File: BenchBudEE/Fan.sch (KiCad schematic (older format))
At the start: 0 parts

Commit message: Fan driver block diagram
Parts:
- added Q?: MOSFET_N, ~, symbol MOSFET_N
- added R? (x5): R, ~, symbol R
- added RV?: POT, ~, symbol POT
- added U?: LM324, symbol LM324
- added U?: MCP4922-E/P, DIP14, symbol MCP4922-E/P
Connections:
- net Fan_In: now also R?.2, R?.2
- net Power+: now also Q?.S
- new net: Q?.G, U?.1
- new net: R?.1, R?.2, R?.2, RV?.3, U?.3 (+)
- new net: R?.1, U?.14 (VoutA)
- new net: R?.1, U?.9 (~SHDN~)
- new net +12V: Q?.D, R?.1, U?.4 (V+)
- new net -12V: U?.11 (V-)
- new net AGND: R?.2, RV?.1
- new net CS_N: U?.3 (~CS~)
- new net Current Measure: R?.1, U?.2 (-)
- new net MOSI: U?.5 (SDI)
- new net SCLK: U?.4 (SCK)

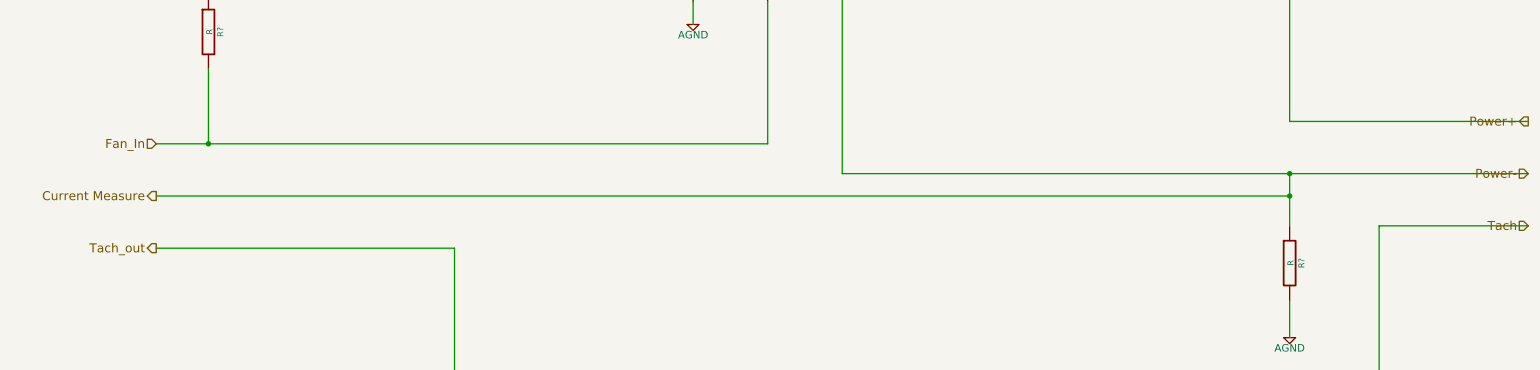
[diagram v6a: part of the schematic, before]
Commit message: Arduino block diagram
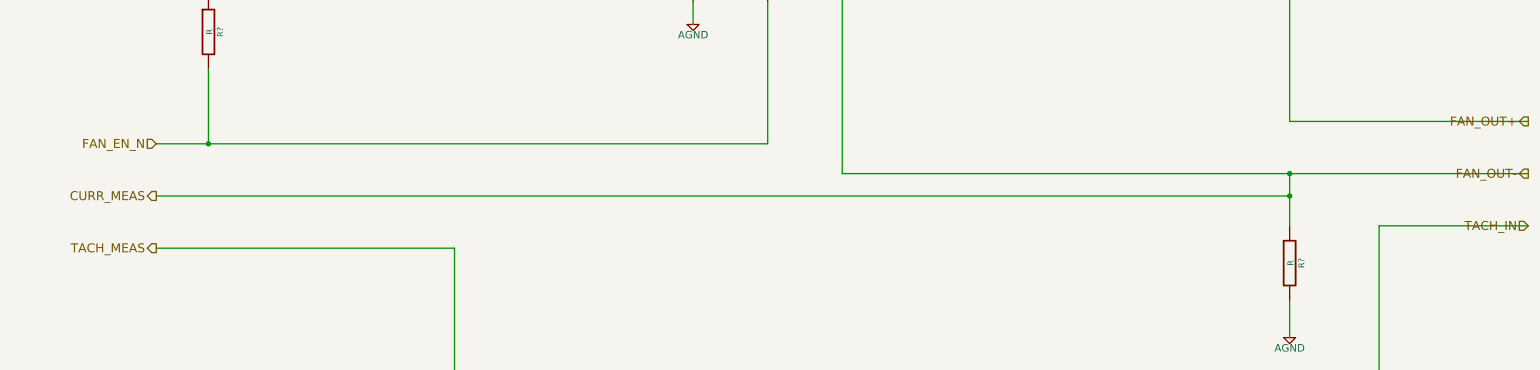
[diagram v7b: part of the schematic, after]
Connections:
- net Current Measure renamed CURR_MEAS
- net Fan_In renamed FAN_EN_N
- net Power+ renamed FAN_OUT+
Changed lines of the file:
@@
 $Descr A4 11693 8268
 encoding utf-8
-Sheet 6 9
+Sheet 8 9
 Title ""
 Date "9 feb 2014"
@@
 $EndDescr
 Text HLabel 10500 4000 0    60   Output ~ 0
-Power+
-Text HLabel 10500 4350 0    60   Input ~ 0
-Power-
+FAN_OUT+
+Text HLabel 10500 4350 0    60   Output ~ 0
+FAN_OUT-
 Text HLabel 10500 4700 0    60   Input ~ 0
-Tach
+TACH_IN
 Text HLabel 1300 4850 0    60   Output ~ 0
-Tach_out
+TACH_MEAS
 Text HLabel 1300 4150 0    60   Input ~ 0
-Fan_In
+FAN_EN_N
 $Comp
 L LM324 U?
@@
 	3300 4850 1300 4850
 Text HLabel 1300 4500 0    60   Output ~ 0
-Current Measure
+CURR_MEAS
 Wire Wire Line
 	8900 4500 1300 4500

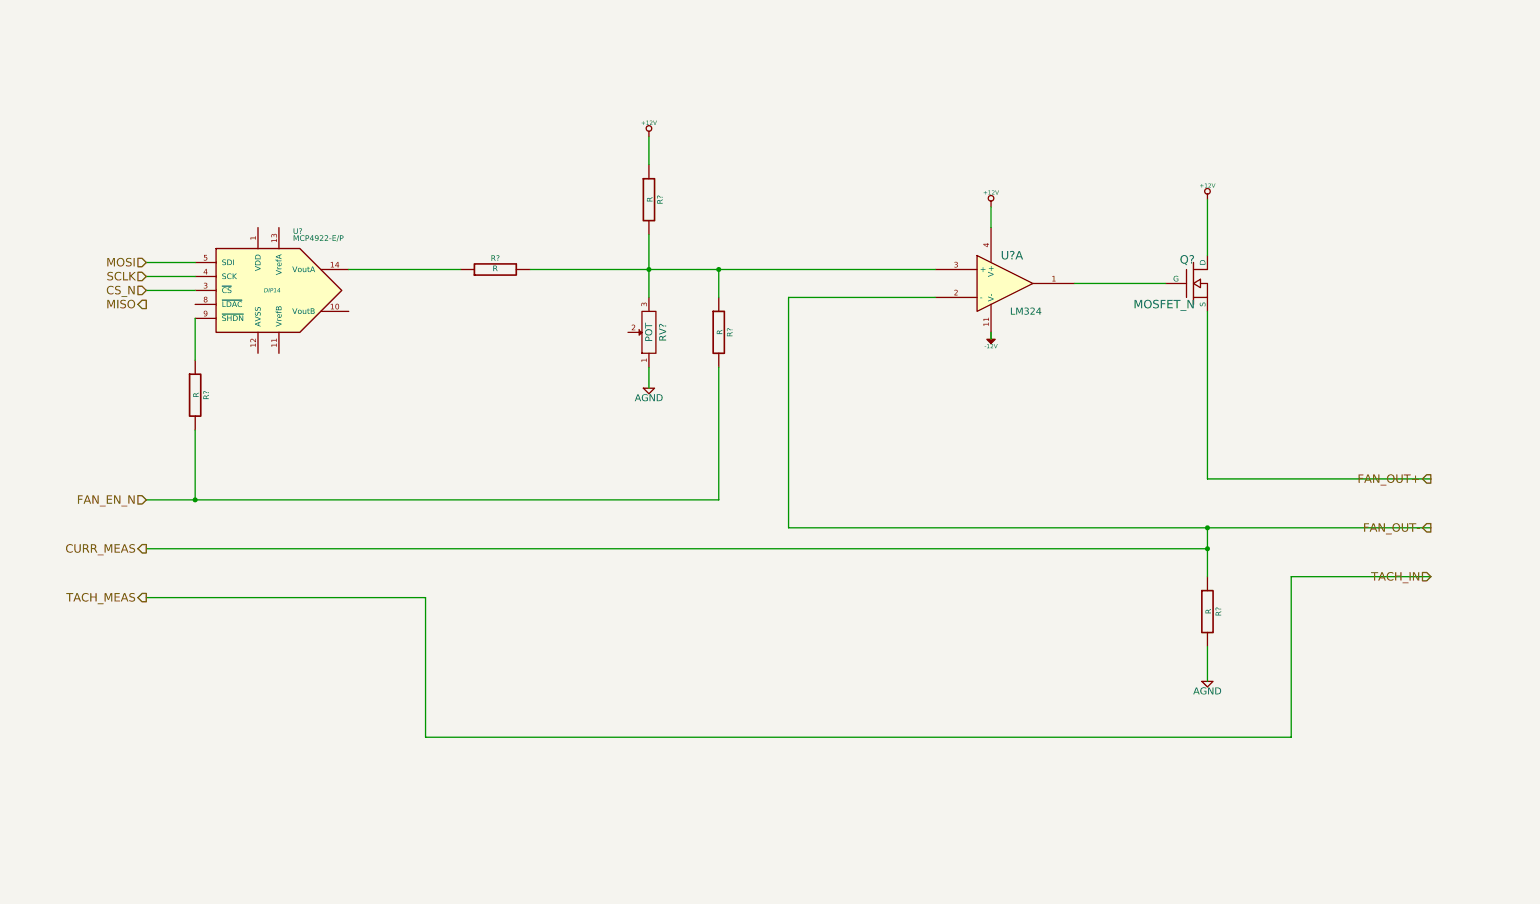
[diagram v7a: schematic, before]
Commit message: Fan/current module refactoring
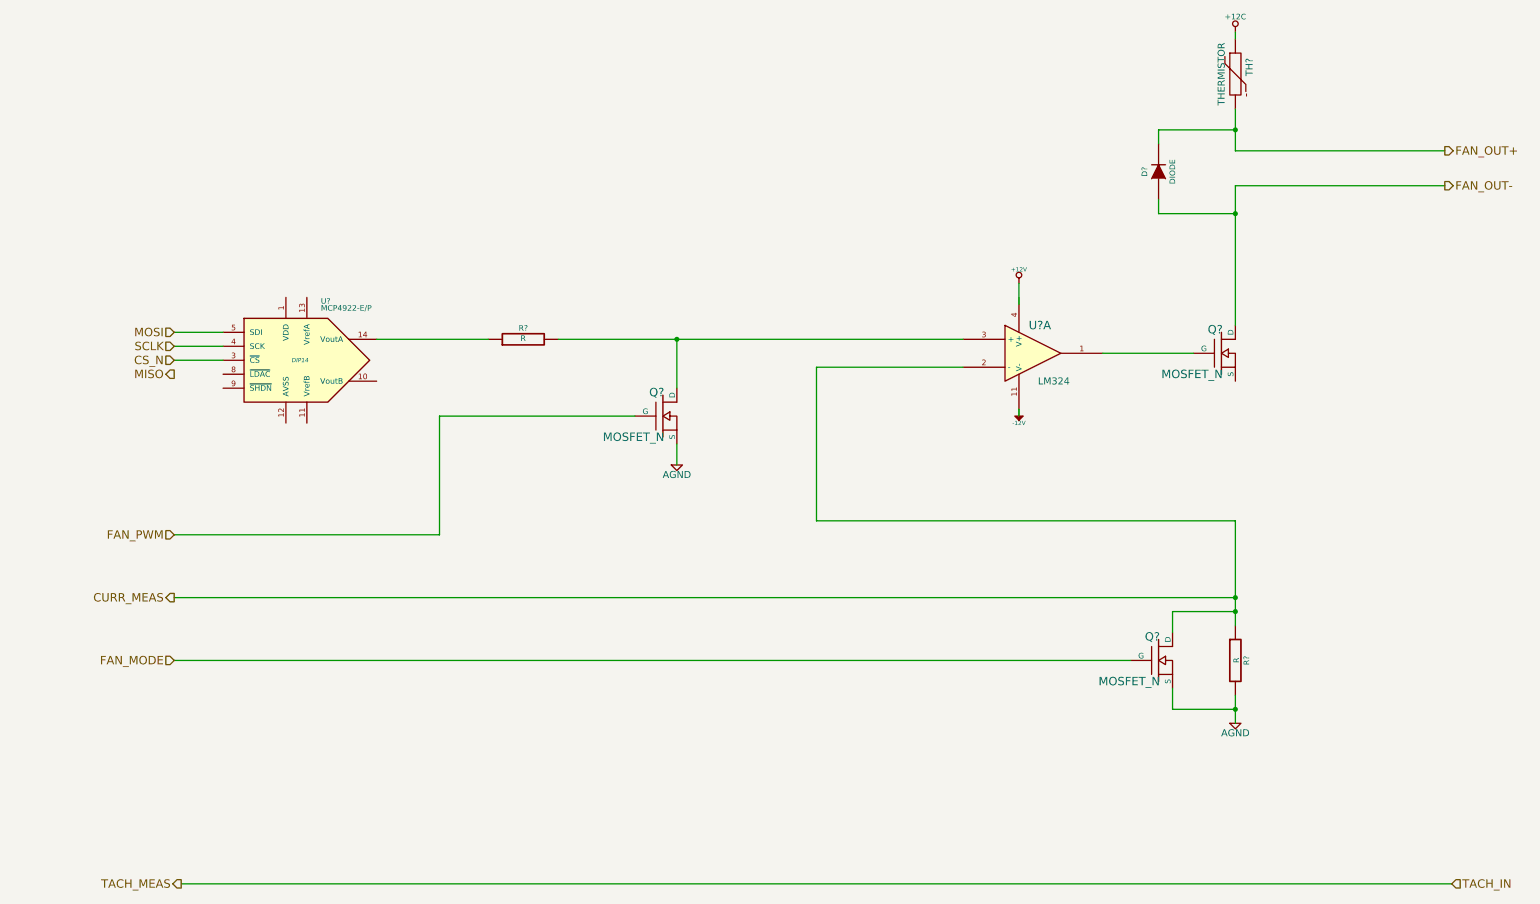
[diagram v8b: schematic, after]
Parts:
- removed R? (x3): R, ~, symbol R
- removed RV?: POT, ~, symbol POT
- added D?: DIODE, ~, symbol DIODE
- added Q? (x2): MOSFET_N, ~, symbol MOSFET_N
- added TH?: THERMISTOR, ~, symbol THERMISTOR
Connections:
- net labels added: +12C, FAN_MODE, FAN_PWM
- net labels removed: FAN_EN_N
- wire segments 30 -> 34
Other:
- moved on the sheet: Q?, R?, U?, U?A
